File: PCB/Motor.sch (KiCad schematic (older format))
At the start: 30 parts

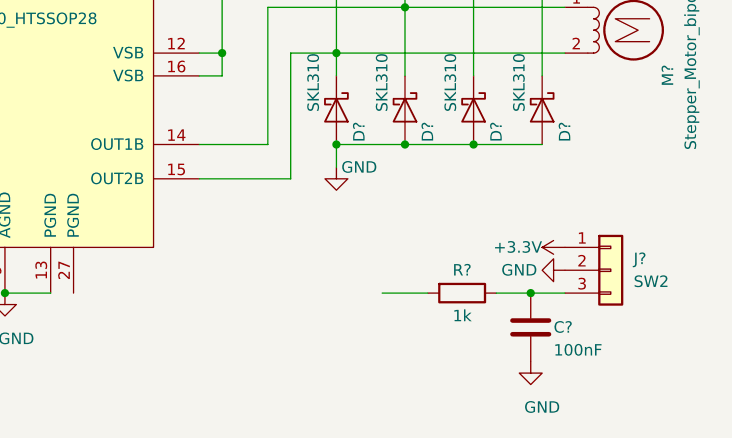
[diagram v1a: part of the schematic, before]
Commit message: Schema: add other motors and create SPI connection
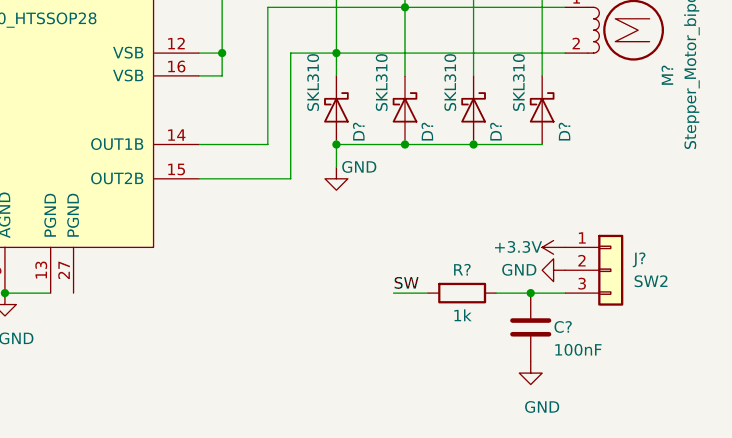
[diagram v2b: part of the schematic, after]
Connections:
- net SW: now also R?.2

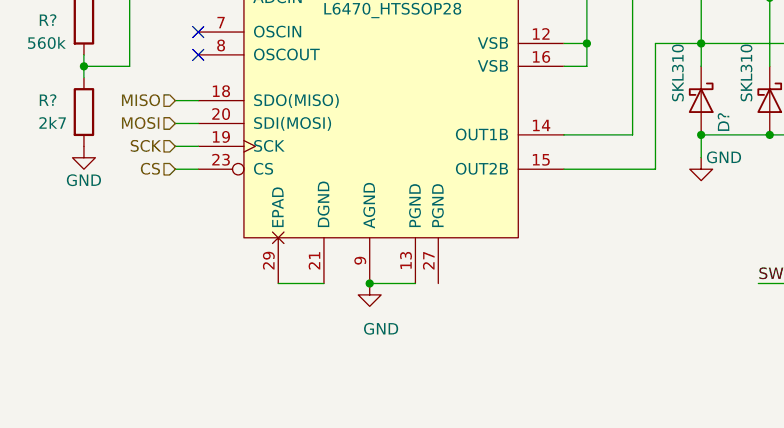
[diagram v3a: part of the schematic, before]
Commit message: Schema: add mcu, RGB LED signalization, reset circuit
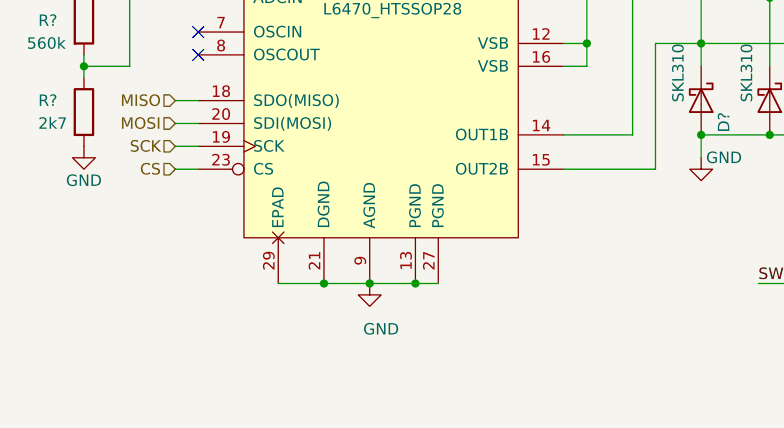
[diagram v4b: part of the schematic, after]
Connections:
- net GND: now also U?.21 (DGND), U?.27 (PGND), U?.29 (EPAD)
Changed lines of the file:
@@
 Wire Wire Line
 	6000 4800 6150 4800
+Wire Wire Line
+	4100 4800 4300 4800
+Connection ~ 4100 4800
+Wire Wire Line
+	4600 4800 4500 4800
+Connection ~ 4500 4800
 $EndSCHEMATC

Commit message: Schema: add FLAG and BUSY LED signalization, fix driver ground connection
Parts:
- C?: symbol Arachne-rescue:C-Device-Motherboard-rescue -> Device:C
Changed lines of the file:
@@
 Connection ~ 6350 2000
 $Comp
-L Arachne-rescue:C-Device-Motherboard-rescue C?
+L Device:C C?
 U 1 1 5D3586AB
 P 6350 2150

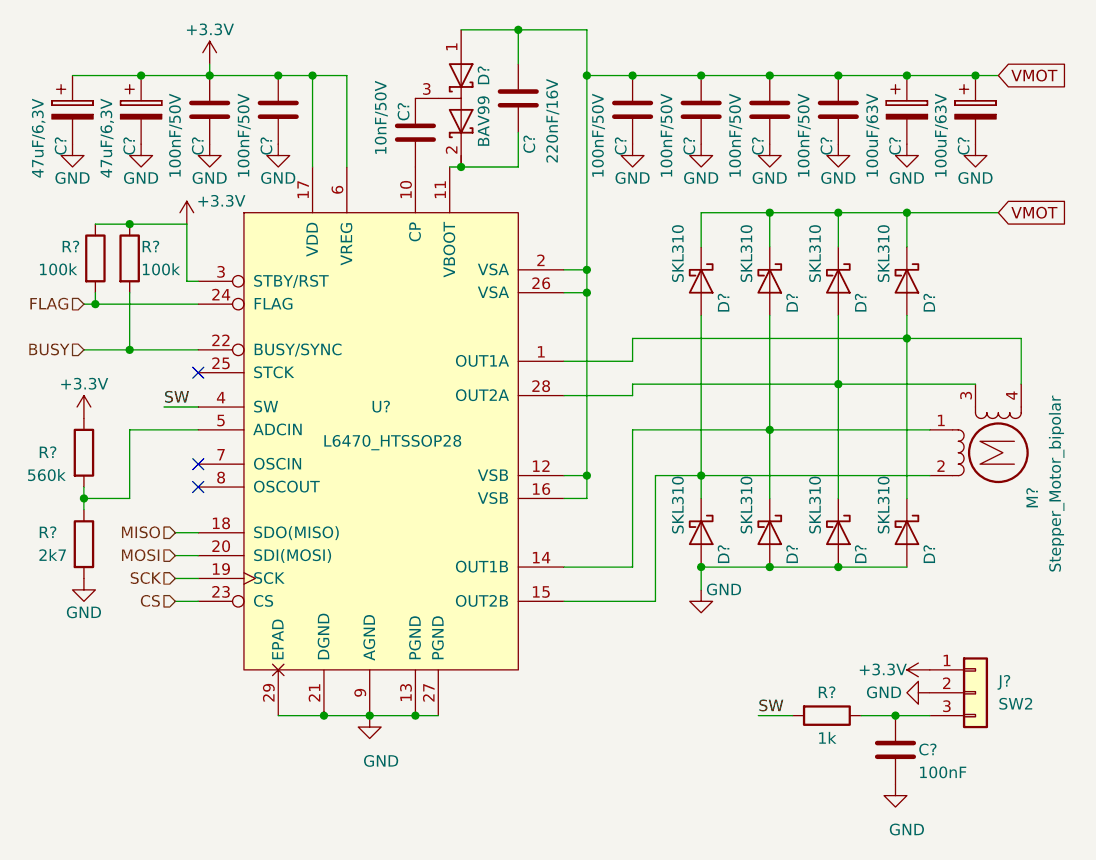
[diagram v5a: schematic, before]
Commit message: Schema: new part annotation, package assignment
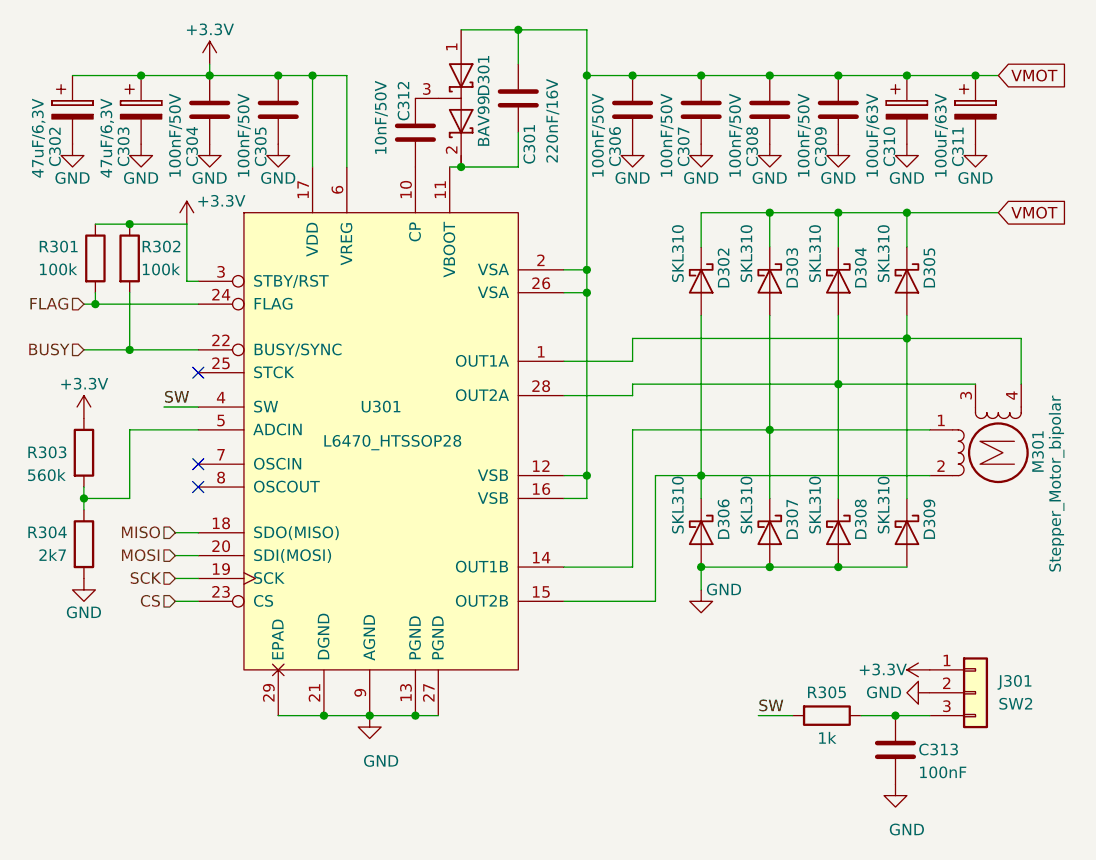
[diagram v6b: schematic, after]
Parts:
- gave numbers to parts that had none: 30

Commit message: PCB: create basic PB layout, add netlist
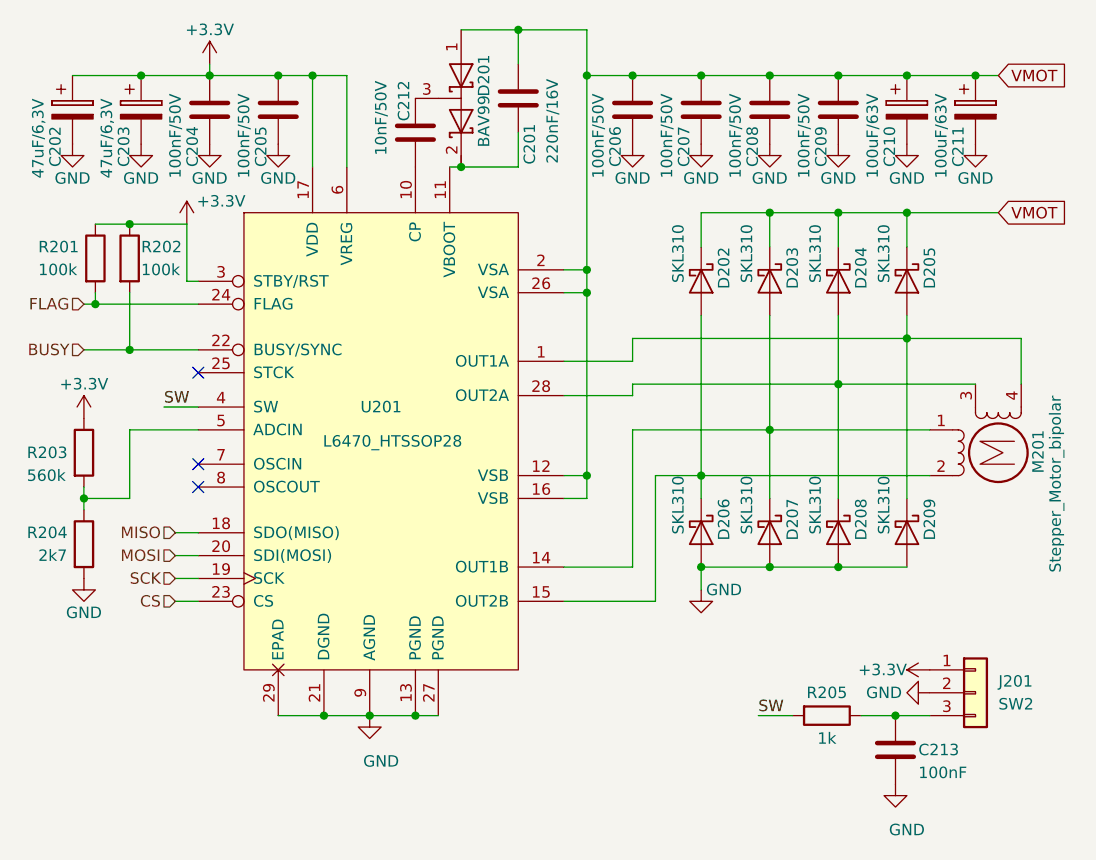
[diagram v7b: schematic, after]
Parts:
- M201: footprint Connector_Phoenix_MC:PhoenixContact_MC_1,5_4-G-3.5_1x04_P3.50mm_Horizontal -> Connector_JST:JST_EH_B4B-EH-A_1x04_P2.50mm_Vertical

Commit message: PCB: routing of first part of stepper motor driver
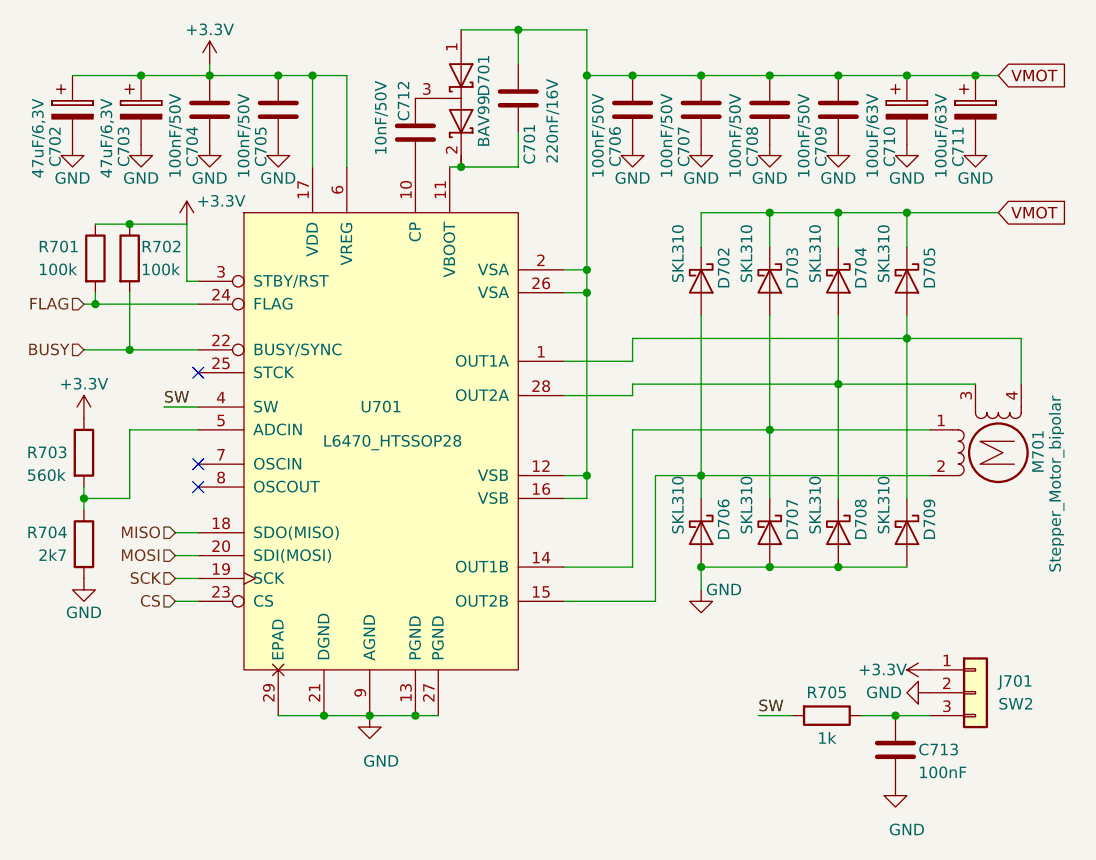
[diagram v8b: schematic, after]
